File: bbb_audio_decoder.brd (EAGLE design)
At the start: 113 x 100 mm, 186 parts, among them IC1 OPA2134, IC2 LM317, IC3 LM337, IC4 OPA2134, IC5 OPA2134, IC6 OPA2134, IC7 LM317, P1 PLR135/T9, Q2 BS170, U1 PCM1690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

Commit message: Connect DIR9001 SCKO to AHCLKR as well.
This is a follow-up of commit c6b4b11, where I apparently only connected
the recovered clock from the DIR9001 to AHCLKX.
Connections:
- net MCLK: now also U$1.28
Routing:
- net MCLK: track 21.8 -> 25.4 mm
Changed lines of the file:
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@@
 <contactref element="U$1" pad="25"/>
 <wire x1="78.105" y1="90.805" x2="80.01" y2="92.71" width="0.254" layer="1"/>
+<contactref element="U$1" pad="28"/>
+<wire x1="80.01" y1="92.71" x2="82.55" y2="95.25" width="0.254" layer="1"/>
 </signal>
 <signal name="N$51">

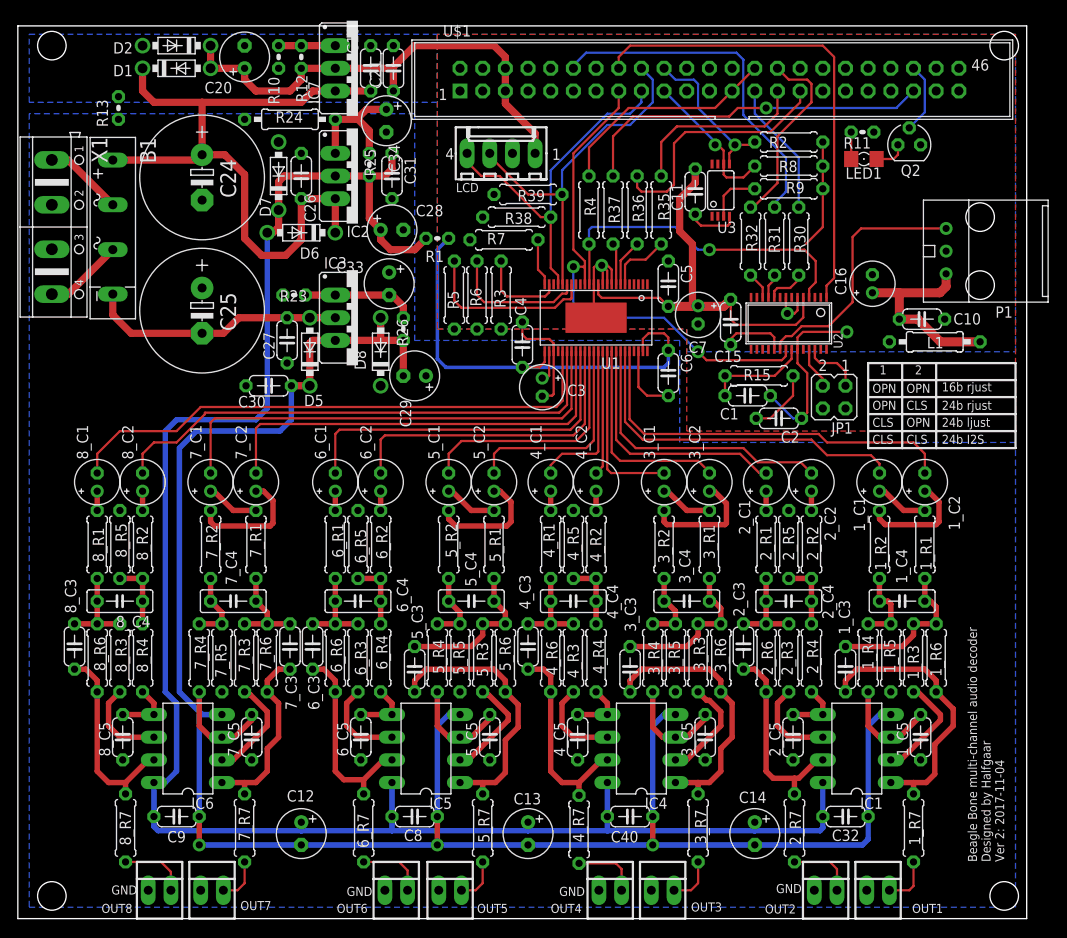
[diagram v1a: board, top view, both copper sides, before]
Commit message: Separate AGND plane in two, to avoid hum
The one large ground plane seemed to cause the charging current for the
main filter caps to circulate around the entire plane, causing the
signal output ground and circuit ground reference to have different
potentials, causing a 100 Hz max hum of -75dBV on some outputs.

This fix breaks the ground plane in two and connects them together with
a small track, to keep the circuit ground clear of those charging
currents.

I wonder if even a 1 Ohm resistor should be used to connect the power
supply ground plane to the circuit ground plane.

This fix hasn't been tested at this point, but it's likely what's
needed.

In the prototype I fixed the hum by cutting the input connector grounds
loose from the ground plane, and wiring them with a dedicated wire to
the circuit ground reference point.
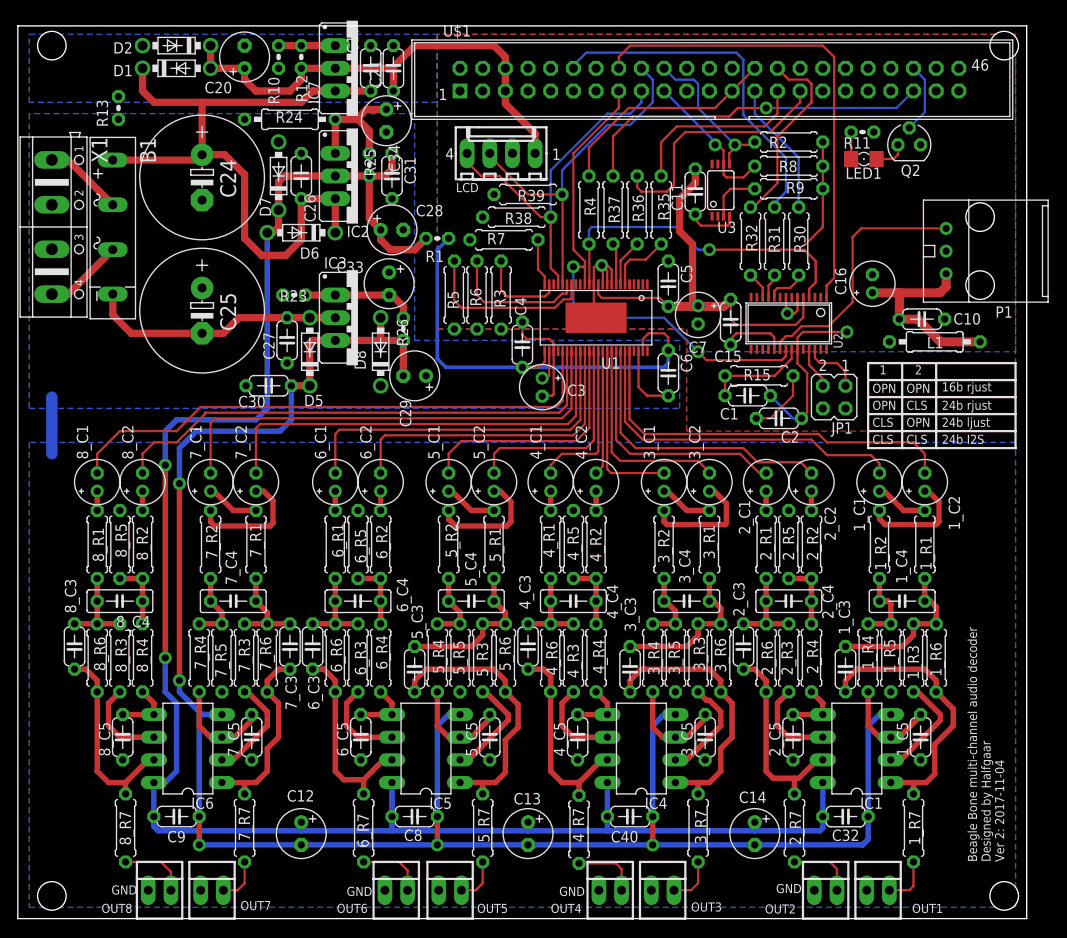
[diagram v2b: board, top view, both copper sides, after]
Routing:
- net AGND: track 20.2 -> 26.5 mm
- net V+: vias 0 -> 2
- net V-: vias 3 -> 5
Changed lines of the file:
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@@
 <polygon width="0.254" layer="16" isolate="0.3048">
 <vertex x="1.27" y="90.17"/>
-<vertex x="1.27" y="1.27"/>
-<vertex x="111.76" y="1.27"/>
-<vertex x="111.76" y="53.34"/>
-<vertex x="74.13625" y="53.34"/>
+<vertex x="1.27" y="57.15"/>
+<vertex x="74.13625" y="57.15"/>
 <vertex x="74.13625" y="64.77"/>
 <vertex x="44.45" y="64.77"/>
@@
 <contactref element="X1" pad="3"/>
 <contactref element="R13" pad="1"/>
+<wire x1="3.81" y1="58.42" x2="3.81" y2="52.07" width="1.27" layer="16"/>
+<polygon width="0.254" layer="16" isolate="0.3048">
+<vertex x="1.27" y="53.34"/>
+<vertex x="1.27" y="1.27"/>
+<vertex x="111.76" y="1.27"/>
+<vertex x="111.76" y="52.07"/>
+<vertex x="111.76" y="53.34"/>
+</polygon>
 </signal>
 <signal name="VCC">
@@
 <wire x1="20.6375" y1="22.86" x2="20.47875" y2="23.01875" width="0.6096" layer="16"/>
 <wire x1="20.47875" y1="23.01875" x2="18.0975" y2="25.4" width="0.6096" layer="16"/>
-<wire x1="18.0975" y1="25.4" x2="18.0975" y2="52.705" width="0.6096" layer="16"/>
 <wire x1="20.32" y1="22.86" x2="20.47875" y2="23.01875" width="0.6096" layer="16"/>
 <via x="20.32" y="8.255" extent="1-16" drill="0.8"/>
@@
 <wire x1="29.36875" y1="54.61" x2="30.63875" y2="55.88" width="0.6096" layer="16"/>
 <wire x1="30.63875" y1="55.88" x2="30.63875" y2="59.69" width="0.6096" layer="16"/>
+<wire x1="18.0975" y1="25.4" x2="18.0975" y2="26.67" width="0.6096" layer="16"/>
+<via x="18.0975" y="26.67" extent="1-16" drill="0.8"/>
+<wire x1="18.0975" y1="26.67" x2="18.0975" y2="48.73625" width="0.6096" layer="1"/>
+<wire x1="18.0975" y1="52.705" x2="18.0975" y2="48.73625" width="0.6096" layer="16"/>
+<via x="18.0975" y="48.73625" extent="1-16" drill="0.8"/>
 </signal>
 <signal name="V+">
@@
 <wire x1="17.78" y1="16.51" x2="17.78" y2="24.13" width="0.6096" layer="16"/>
 <wire x1="17.78" y1="24.13" x2="16.51" y2="25.4" width="0.6096" layer="16"/>
-<wire x1="16.51" y1="54.61" x2="16.51" y2="25.4" width="0.6096" layer="16"/>
 <contactref element="C12" pad="+"/>
 <contactref element="C13" pad="+"/>
@@
 <wire x1="39.37" y1="83.185" x2="39.37" y2="78.4225" width="0.8128" layer="1"/>
 <wire x1="39.37" y1="78.4225" x2="40.64" y2="77.1525" width="0.8128" layer="1"/>
+<wire x1="16.51" y1="54.61" x2="16.51" y2="50.8" width="0.6096" layer="16"/>
+<wire x1="16.51" y1="25.4" x2="16.51" y2="29.21" width="0.6096" layer="16"/>
+<via x="16.51" y="29.21" extent="1-16" drill="0.8"/>
+<wire x1="16.51" y1="29.21" x2="16.51" y2="50.8" width="0.6096" layer="1"/>
+<via x="16.51" y="50.8" extent="1-16" drill="0.8"/>
 </signal>
 <signal name="N$39">
